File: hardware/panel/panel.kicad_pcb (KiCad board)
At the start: 2 copper layers, 70.8 x 128.5 mm, 34 parts

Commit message: Update datestamps, version numbers, and order new boards
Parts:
- removed the G*** at (86.6, 110.6) (x3)
- added G*** (x3): LOGO, LOGO, F.Cu at (86.6, 110.6)
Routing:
- added copper zone on B.Cu, net (none)
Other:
- board text added: "Castor & Pollux v1 9/7/2020 wntr.dev/gemini"

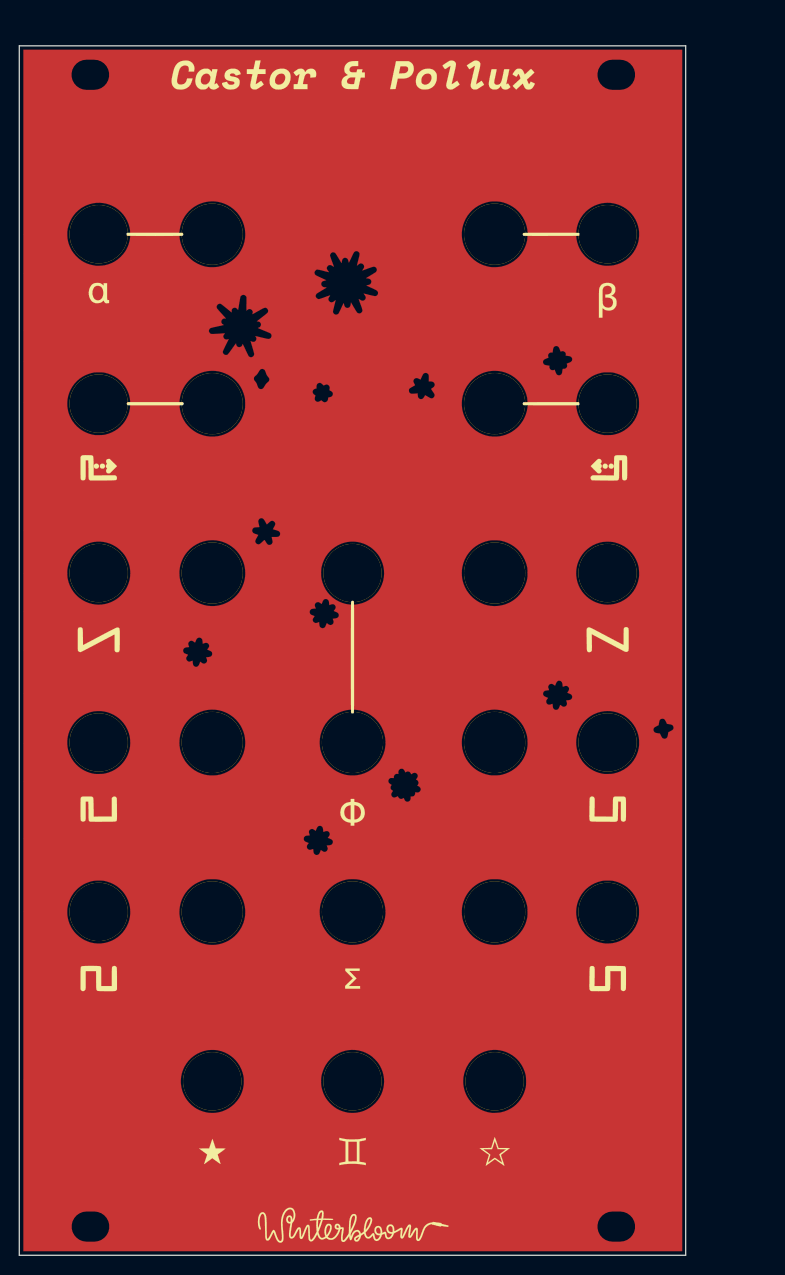
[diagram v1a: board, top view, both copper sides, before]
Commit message: Update panel for hard sync
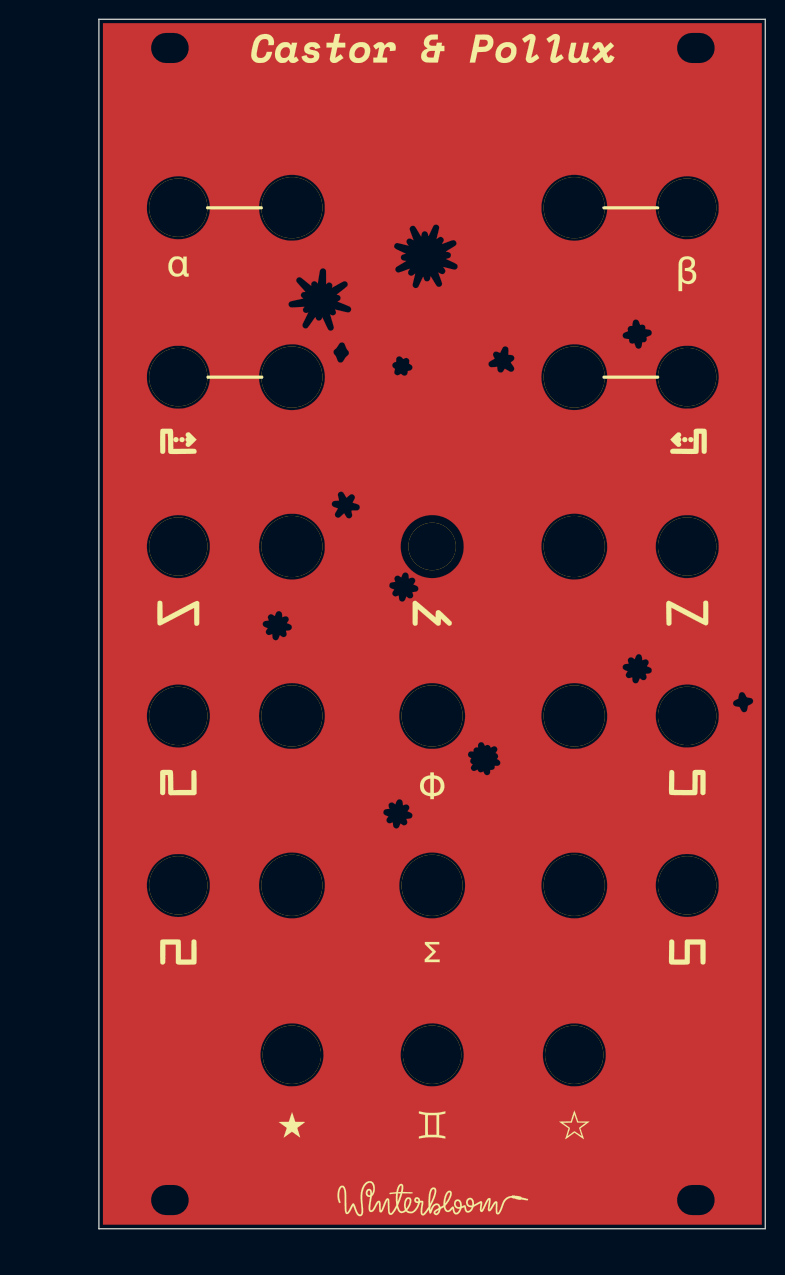
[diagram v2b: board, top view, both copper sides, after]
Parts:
- removed the   at (114.6, 171.8)
- removed the   at (114.6, 49.4)
- removed the   at (58.8, 171.8)
- removed the   at (58.8, 49.4)
- removed the ? at (71.7, 120.4)
- removed the ? at (71.7, 66.4)
- removed the ? at (59.6, 84.4)
- removed the ? at (71.7, 84.4)
- removed the ? at (101.7, 120.4)
- removed the ? at (101.7, 138.4)
- removed the ? at (101.7, 102.4)
- removed the ? at (113.7, 66.4)
- removed the ? at (101.7, 156.4)
- removed the ? at (113.7, 138.4)
- removed the ? at (113.7, 120.4)
- removed the ? at (71.7, 138.4)
- removed the ? at (86.6, 102.4)
- removed the ? at (113.7, 102.4)
- removed the ? at (101.7, 66.4)
- removed the ? at (113.7, 84.4)
- removed the ? at (101.7, 84.4)
- removed the ? at (86.6, 138.4)
- removed the ? at (86.6, 156.4)
- removed the ? at (71.7, 102.4)
- removed the ? at (86.6, 120.4)
- removed the ? at (59.6, 66.4)
- removed the ? at (71.7, 156.4)
- removed the ? at (59.6, 138.4)
- removed the ? at (59.6, 120.4)
- removed the ? at (59.6, 102.4)
- removed the G*** at (86.6, 110.6) (x4)
- added  : , panel:MountingHoleEurorackSlotM3, F.Cu at (123.1, 169.0)
- added  : , panel:MountingHoleEurorackSlotM3, F.Cu at (123.1, 46.6)
- added  : , panel:MountingHoleEurorackSlotM3, F.Cu at (67.2, 169.0)
- added  : , panel:MountingHoleEurorackSlotM3, F.Cu at (67.2, 46.6)
- added ?: , Wire_Pads:SolderWirePad_single_0-8mmDrill, F.Cu at (95.1, 99.5)
- added ?: , Wire_Pads:SolderWirePad_single_0-8mmDrill, F.Cu at (68.1, 99.5)
- added ?: , Wire_Pads:SolderWirePad_single_0-8mmDrill, F.Cu at (80.2, 63.5)
- added ?: , Wire_Pads:SolderWirePad_single_0-8mmDrill, F.Cu at (68.1, 81.5)
- added ?: , Wire_Pads:SolderWirePad_single_0-8mmDrill, F.Cu at (80.2, 81.5)
- added ?: , Wire_Pads:SolderWirePad_single_0-8mmDrill, F.Cu at (110.2, 117.5)
- added ?: , Wire_Pads:SolderWirePad_single_0-8mmDrill, F.Cu at (110.2, 135.5)
- added ?: , Wire_Pads:SolderWirePad_single_0-8mmDrill, F.Cu at (110.2, 99.5)
- added ?: , Wire_Pads:SolderWirePad_single_0-8mmDrill, F.Cu at (122.2, 63.5)
- added ?: , Wire_Pads:SolderWirePad_single_0-8mmDrill, F.Cu at (110.2, 153.5)
- added ?: , Wire_Pads:SolderWirePad_single_0-8mmDrill, F.Cu at (122.2, 135.5)
- added ?: , Wire_Pads:SolderWirePad_single_0-8mmDrill, F.Cu at (80.2, 117.5)
- added ?: , Wire_Pads:SolderWirePad_single_0-8mmDrill, F.Cu at (122.2, 117.5)
- added ?: , Wire_Pads:SolderWirePad_single_0-8mmDrill, F.Cu at (122.2, 99.5)
- added ?: , Wire_Pads:SolderWirePad_single_0-8mmDrill, F.Cu at (110.2, 63.5)
- added ?: , Wire_Pads:SolderWirePad_single_0-8mmDrill, F.Cu at (122.2, 81.5)
- added ?: , Wire_Pads:SolderWirePad_single_0-8mmDrill, F.Cu at (110.2, 81.5)
- added ?: , Wire_Pads:SolderWirePad_single_0-8mmDrill, F.Cu at (95.1, 135.5)
- added ?: , Wire_Pads:SolderWirePad_single_0-8mmDrill, F.Cu at (95.1, 153.5)
- added ?: , Wire_Pads:SolderWirePad_single_0-8mmDrill, F.Cu at (80.2, 135.5)
- added ?: , Wire_Pads:SolderWirePad_single_0-8mmDrill, F.Cu at (80.2, 99.5)
- added ?: , Wire_Pads:SolderWirePad_single_0-8mmDrill, F.Cu at (95.1, 117.5)
- added ?: , Wire_Pads:SolderWirePad_single_0-8mmDrill, F.Cu at (68.1, 63.5)
- added ?: , Wire_Pads:SolderWirePad_single_0-8mmDrill, F.Cu at (80.2, 153.5)
- added ?: , Wire_Pads:SolderWirePad_single_0-8mmDrill, F.Cu at (68.1, 135.5)
- added ?: , Wire_Pads:SolderWirePad_single_0-8mmDrill, F.Cu at (68.1, 117.5)
- added G*** (x4): LOGO, LOGO, F.Cu at (95.1, 107.8)
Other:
- board text added: "Castor & Pollux v2 9/25/2020 wntr.dev/gemini"
- board text removed: "Black substrate Black soldermask White silkscreen ENIG plating"
- board text removed: "Castor & Pollux v1 9/7/2020 wntr.dev/gemini"

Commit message: Once again I find myself unsure of what KiCAD did here.
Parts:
- removed the G*** at (95.1, 107.8) (x4)
- added G*** (x4): LOGO, LOGO, F.Cu at (95.1, 107.8)

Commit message: Update panel pcb after preparing gerbers
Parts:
- removed the G*** at (95.1, 107.8) (x4)
- added G*** (x4): LOGO, LOGO, F.Cu at (95.1, 107.8)

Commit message: Thoroughly document all applicable licenses
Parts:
- removed the G*** at (95.1, 107.8) (x4)
- added G*** (x4): LOGO, LOGO, F.Cu at (95.1, 107.8)
